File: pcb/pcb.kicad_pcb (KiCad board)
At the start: 2 copper layers, 69.8 x 75.4 mm, 69 parts, among them J1 USB_C_Receptacle_USB2.0, J2 Conn_01x05, SW1 SW_Push, SW2 SW_Push, U1 SRV05-4, U10 RP2040, U11 W25Q128JVS, U2 XC6206P332MR, U3 DRV5056A3xDBZxQ1, U4 DRV5056A3xDBZxQ1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

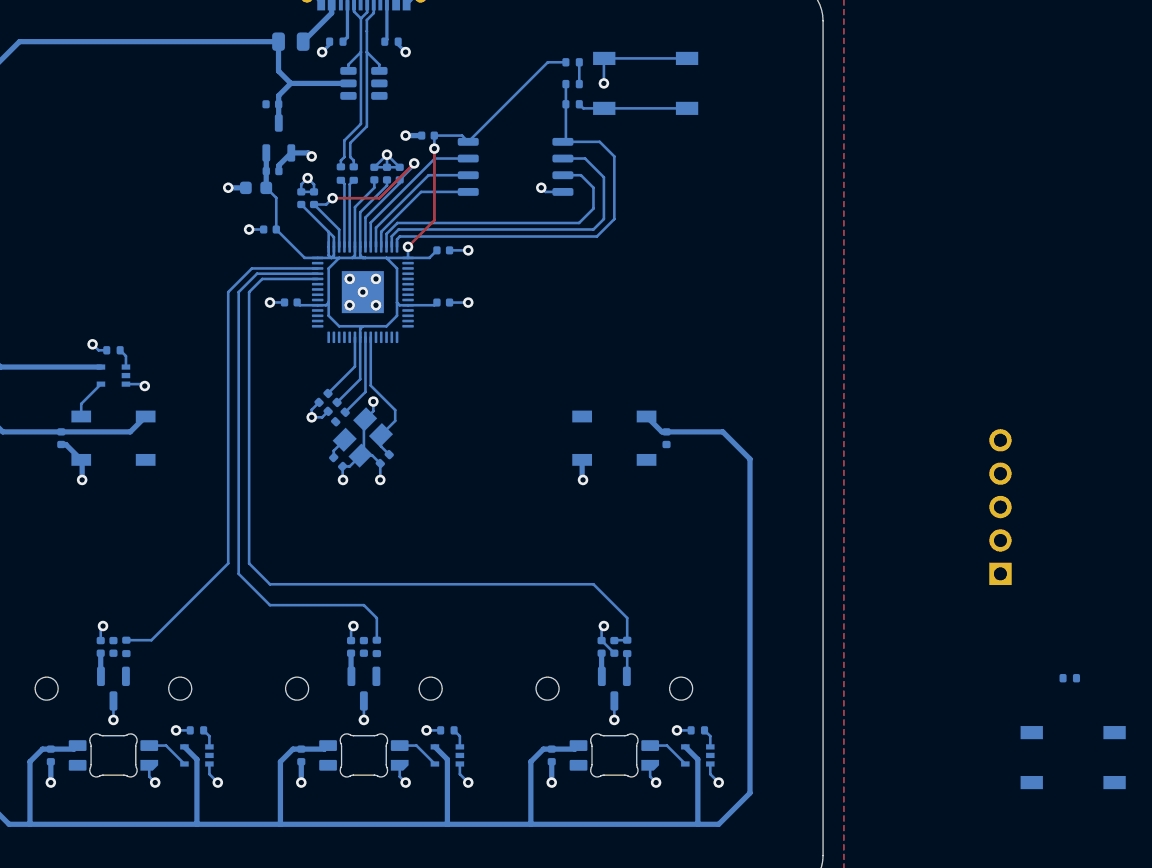
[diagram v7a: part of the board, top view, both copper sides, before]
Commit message: feat: fully connected pcb
ended up removing the debug header - I don't think these appear in production boards anyway, so should be OK.

there's probably a better way to route the analog lines, but I couldn't come up with anything for it...
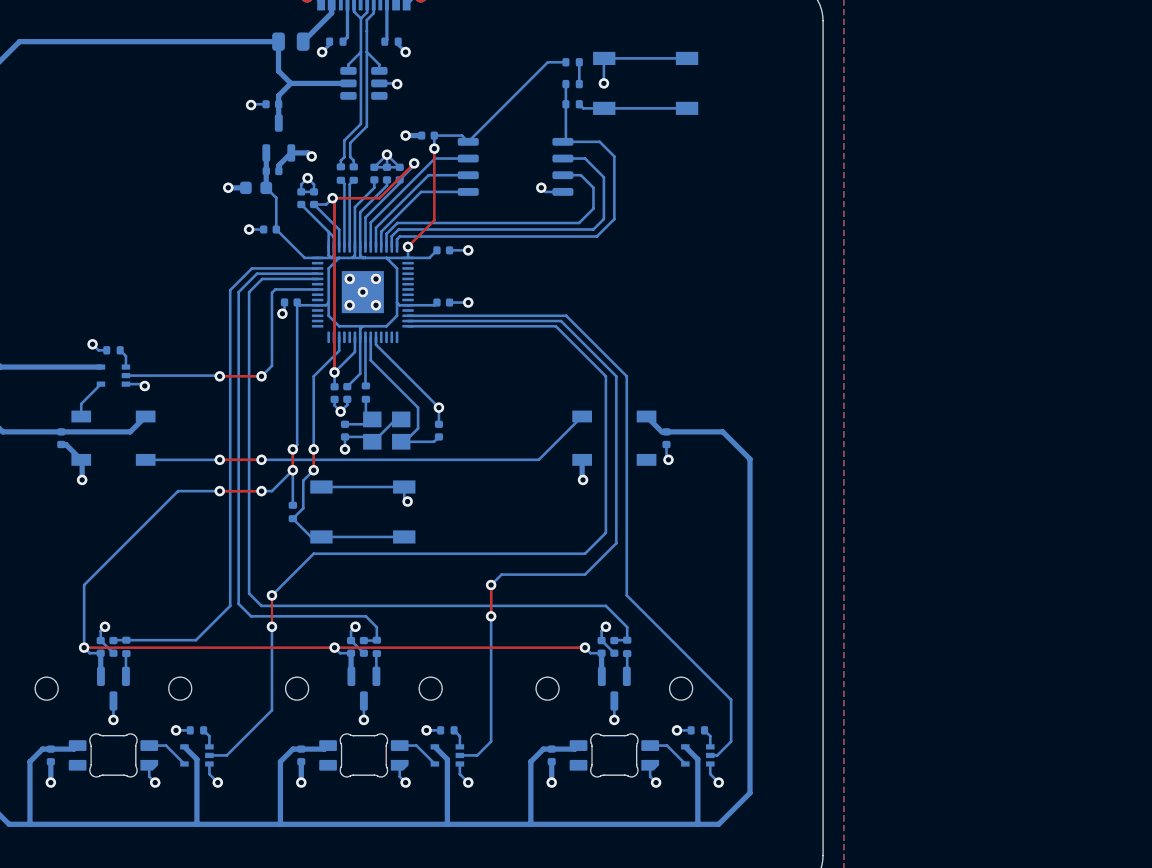
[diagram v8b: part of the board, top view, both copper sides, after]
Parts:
- removed J2: Conn_01x05, Connector_PinHeader_2.54mm:PinHeader_1x05_P2.54mm_Horizontal
- moved R14 60.4 mm to (53.3, 72.3), turned to -90 degrees
- moved SW1 57.2 mm to (58.7, 72.3)
- moved C24 4.65 mm to (64.4, 66.1), turned to -90 degrees
- moved R9 2.68 mm to (58.9, 63.2), turned to 90 degrees
- moved C25 2.44 mm to (57.3, 66.1), turned to 90 degrees
- moved Y1 1.89 mm to (60.5, 66.1), turned to 0 degrees
- moved C23 1.54 mm to (57.5, 63.2), turned to -90 degrees
- moved C13 0.92 mm to (56.5, 63.2), turned to -90 degrees
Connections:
- U10 pad 12: unconnected-(U10-GPIO9-Pad12) -> RGB_HS2
- U10 pad 13: unconnected-(U10-GPIO10-Pad13) -> RGB_HS1
- U10 pad 14: unconnected-(U10-GPIO11-Pad14) -> RGB_HS0
- U10 pad 2: RGB_GLOW -> unconnected-(U10-GPIO0-Pad2)
- U10 pad 3: RGB_HS0 -> unconnected-(U10-GPIO1-Pad3)
- U10 pad 36: unconnected-(U10-GPIO24-Pad36) -> RGB_GLOW
- U10 pad 4: RGB_HS1 -> unconnected-(U10-GPIO2-Pad4)
- U10 pad 5: RGB_HS2 -> unconnected-(U10-GPIO3-Pad5)
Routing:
- net +3V3: track 96.3 -> 177.1 mm, vias 2 -> 9
- net RGB_HS0: track 0.00 -> 70.8 mm, vias 0 -> 2
- net RGB_HS1: track 0.00 -> 55.8 mm, vias 0 -> 2
- net RGB_HS2: track 0.00 -> 51.6 mm
- net Net-(D1-DOUT): track 0.13 -> 34.7 mm, vias 0 -> 2
- net RESET: track 0.00 -> 24.3 mm, vias 0 -> 2
- net RGB_GLOW: track 0.00 -> 20.6 mm, vias 0 -> 2
- net GND: track 99.8 -> 117.5 mm, vias 44 -> 47
- net +1V1: track 25.9 -> 38.5 mm, vias 2 -> 3
- net HS0: track 38.4 -> 41.3 mm
- net XIN: track 10.4 -> 13.2 mm
- net XOUT: track 6.34 -> 3.71 mm
- net Net-(C25-Pad2): track 1.70 -> 3.96 mm
- net HS1: track 41.6 -> 43.5 mm
- net Net-(U4-OUT): track 0.00 -> 1.74 mm
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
